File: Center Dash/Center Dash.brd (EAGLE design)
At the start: 159 x 86.7 mm, 82 parts, among them J1 502585-0470, Q1 BSS138, Q2 BSS138, Q3 BSS138, Q4 BSS138, U1 ADG3304BRUZ-REEL7, U2 TPS54540DDARQ1

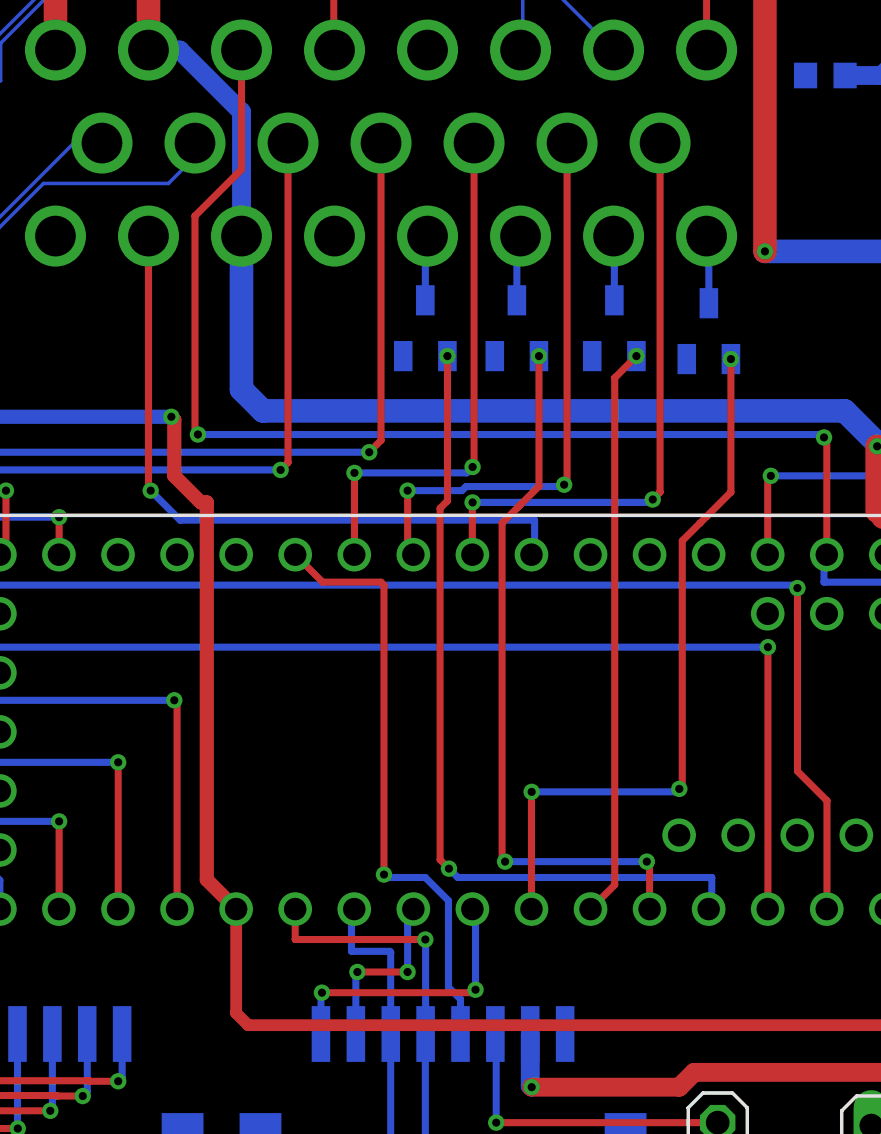
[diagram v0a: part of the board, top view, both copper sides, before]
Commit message: Add voltage dividers to 5V input lines
Now we can use Teensy 3.6
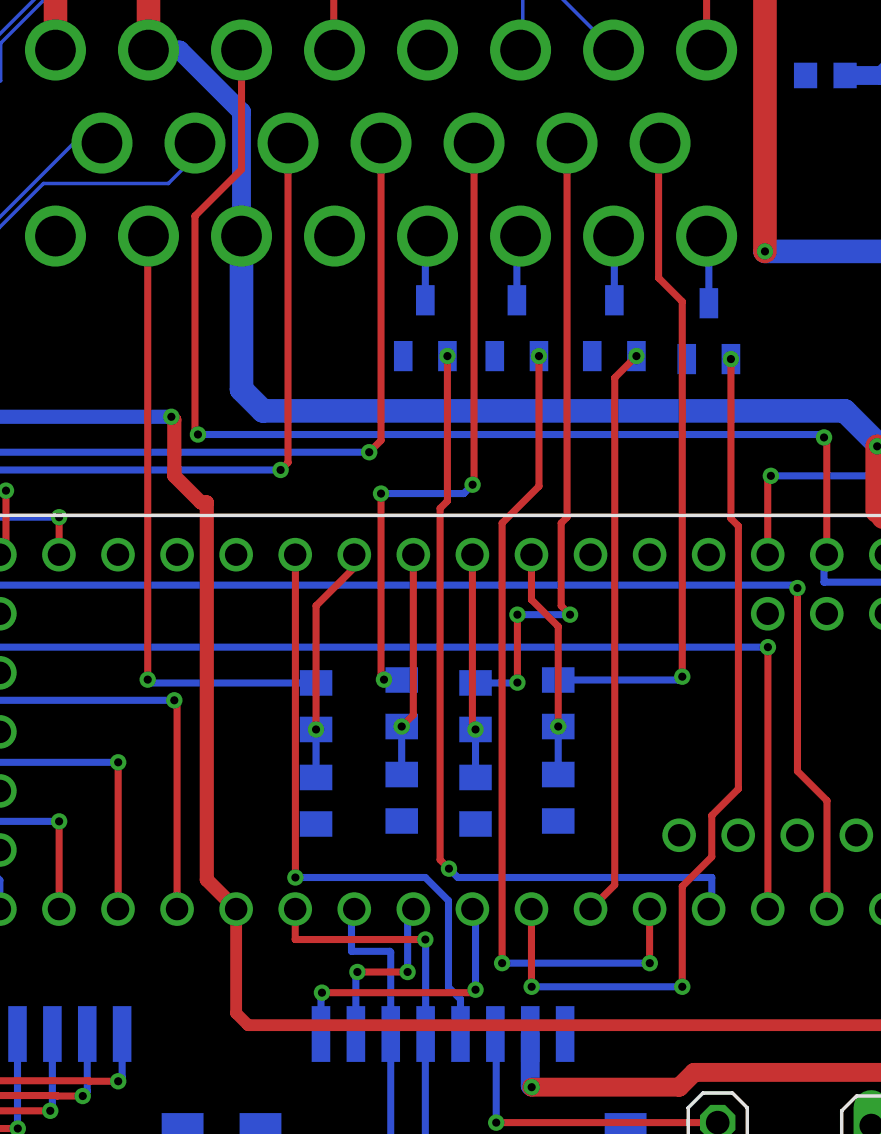
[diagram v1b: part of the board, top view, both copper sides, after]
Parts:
- added R17, R19, R21, R23: 1K, adafruit:R0805
- added R18, R20, R22, R24: 2K, adafruit:R0805
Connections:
- new net SW_BIT0_IN: R17.2, U$1.P$17
- new net SW_BIT1_IN: R19.2, U$1.P$13
- new net SW_BIT2_IN: R21.2, U$1.P$14
- new net SW_BIT3_IN: R23.2, U$1.P$15
- net GND: now also R18.1, R20.1, R22.1, R24.1
- net SW_BIT0: now also R17.1, R18.2; no longer U$1.P$13
- net SW_BIT1: now also R19.1, R20.2; no longer U$1.P$14
- net SW_BIT2: now also R21.1, R22.2; no longer U$1.P$15
- net SW_BIT3: now also R23.1, R24.2; no longer U$1.P$17
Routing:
- net SW_BIT3_IN: track 0.00 -> 28.8 mm, vias 0 -> 1
- net SW_BIT1_IN: track 0.00 -> 27.6 mm, vias 0 -> 3
- net SW_BIT2_IN: track 0.00 -> 27.5 mm, vias 0 -> 3
- net SW_BIT0_IN: track 0.00 -> 26.4 mm, vias 0 -> 1
- net SW_BIT3: track 29.6 -> 9.93 mm
- net SW_BIT2: track 25.5 -> 9.64 mm, vias 2 -> 1
- net SW_BIT1: track 24.4 -> 9.66 mm, vias 2 -> 1
- net SW_BIT0: track 22.7 -> 10.3 mm, vias 2 -> 1
- net TPS: track 30.9 -> 37.9 mm
- net IMD: track 30.6 -> 35.4 mm
- net CLK: track 26.0 -> 26.8 mm

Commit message: last minute fix again
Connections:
- net +3V3: now also U1.8
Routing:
- net +3V3: track 180.1 -> 188.9 mm
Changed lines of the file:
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@@
 <wire x1="-28.067" y1="74.422" x2="-28.067" y2="76.134" width="0.6096" layer="16"/>
 <wire x1="-28.067" y1="76.134" x2="-28.895" y2="76.962" width="0.6096" layer="16"/>
+<contactref element="U1" pad="8"/>
+<wire x1="38.252" y1="59.608" x2="36.494" y2="59.608" width="0.3048" layer="16"/>
+<wire x1="36.494" y1="59.608" x2="35.814" y2="58.928" width="0.3048" layer="16"/>
+<wire x1="35.814" y1="58.928" x2="35.814" y2="57.658" width="0.3048" layer="16"/>
+<wire x1="35.814" y1="57.658" x2="34.671" y2="56.515" width="0.3048" layer="16"/>
+<wire x1="34.671" y1="56.515" x2="34.417" y2="56.261" width="0.3048" layer="16"/>
+<wire x1="31.852" y1="55.708" x2="33.864" y2="55.708" width="0.3048" layer="16"/>
+<wire x1="33.864" y1="55.708" x2="34.417" y2="56.261" width="0.3048" layer="16"/>
 </signal>
 <signal name="PADDLE">
@@
 <wire x1="36.957" y1="52.578" x2="36.957" y2="57.277" width="0.3048" layer="1"/>
 <wire x1="36.957" y1="57.277" x2="35.941" y2="58.293" width="0.3048" layer="1"/>
-<via x="35.941" y="58.293" extent="1-16" drill="0.35"/>
-<wire x1="35.941" y1="58.293" x2="31.867" y2="58.293" width="0.3048" layer="16"/>
-<wire x1="31.867" y1="58.293" x2="31.852" y2="58.308" width="0.3048" layer="16"/>
+<wire x1="35.941" y1="58.293" x2="35.9184" y2="58.2704" width="0.3048" layer="1"/>
+<wire x1="35.9184" y1="58.2704" x2="34.544" y2="58.2704" width="0.3048" layer="1"/>
+<via x="34.544" y="58.2704" extent="1-16" drill="0.35"/>
+<wire x1="34.544" y1="58.2704" x2="31.8896" y2="58.2704" width="0.3048" layer="16"/>
+<wire x1="31.8896" y1="58.2704" x2="31.852" y2="58.308" width="0.3048" layer="16"/>
 </signal>
 <signal name="DI">
@@
 <wire x1="30.226" y1="63.5" x2="30.419" y2="63.693" width="0.3048" layer="1"/>
 <wire x1="30.419" y1="63.693" x2="31.877" y2="63.693" width="0.3048" layer="1"/>
-<via x="36.83" y="58.928" extent="1-16" drill="0.35"/>
-<wire x1="36.83" y1="58.928" x2="36.8" y2="58.958" width="0.3048" layer="16"/>
-<wire x1="36.8" y1="58.958" x2="31.852" y2="58.958" width="0.3048" layer="16"/>
 <contactref element="JP5" pad="1"/>
 <wire x1="39.497" y1="52.578" x2="39.497" y2="58.801" width="0.3048" layer="1"/>
 <wire x1="39.497" y1="58.801" x2="39.37" y2="58.928" width="0.3048" layer="1"/>
-<wire x1="39.37" y1="58.928" x2="36.83" y2="58.928" width="0.3048" layer="1"/>
+<via x="33.655" y="58.928" extent="1-16" drill="0.35"/>
+<wire x1="33.655" y1="58.928" x2="33.625" y2="58.958" width="0.3048" layer="16"/>
+<wire x1="33.625" y1="58.958" x2="31.852" y2="58.958" width="0.3048" layer="16"/>
+<wire x1="39.37" y1="58.928" x2="33.655" y2="58.928" width="0.3048" layer="1"/>
 </signal>
 <signal name="DI_MORE">

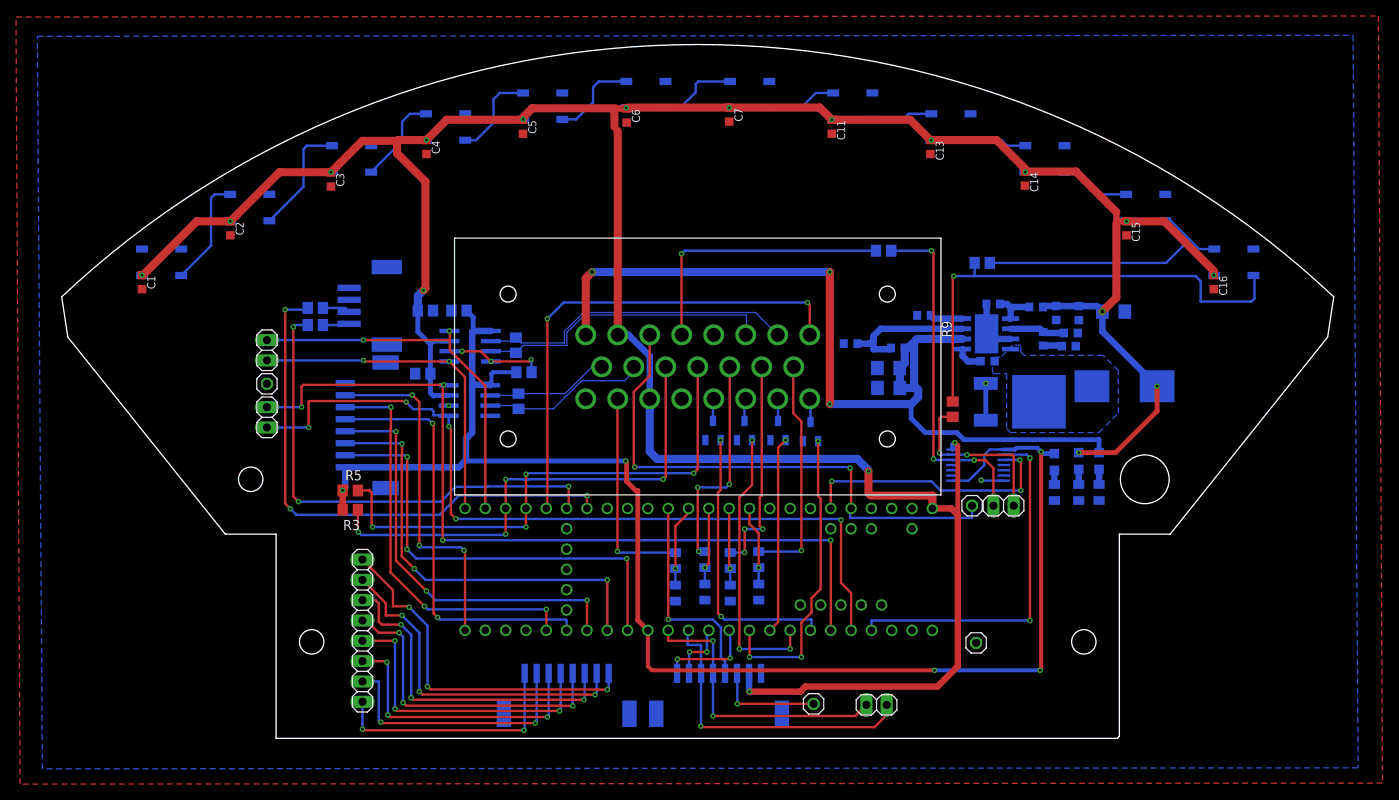
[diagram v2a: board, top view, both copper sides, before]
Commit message: Fixed?? amp seal connector
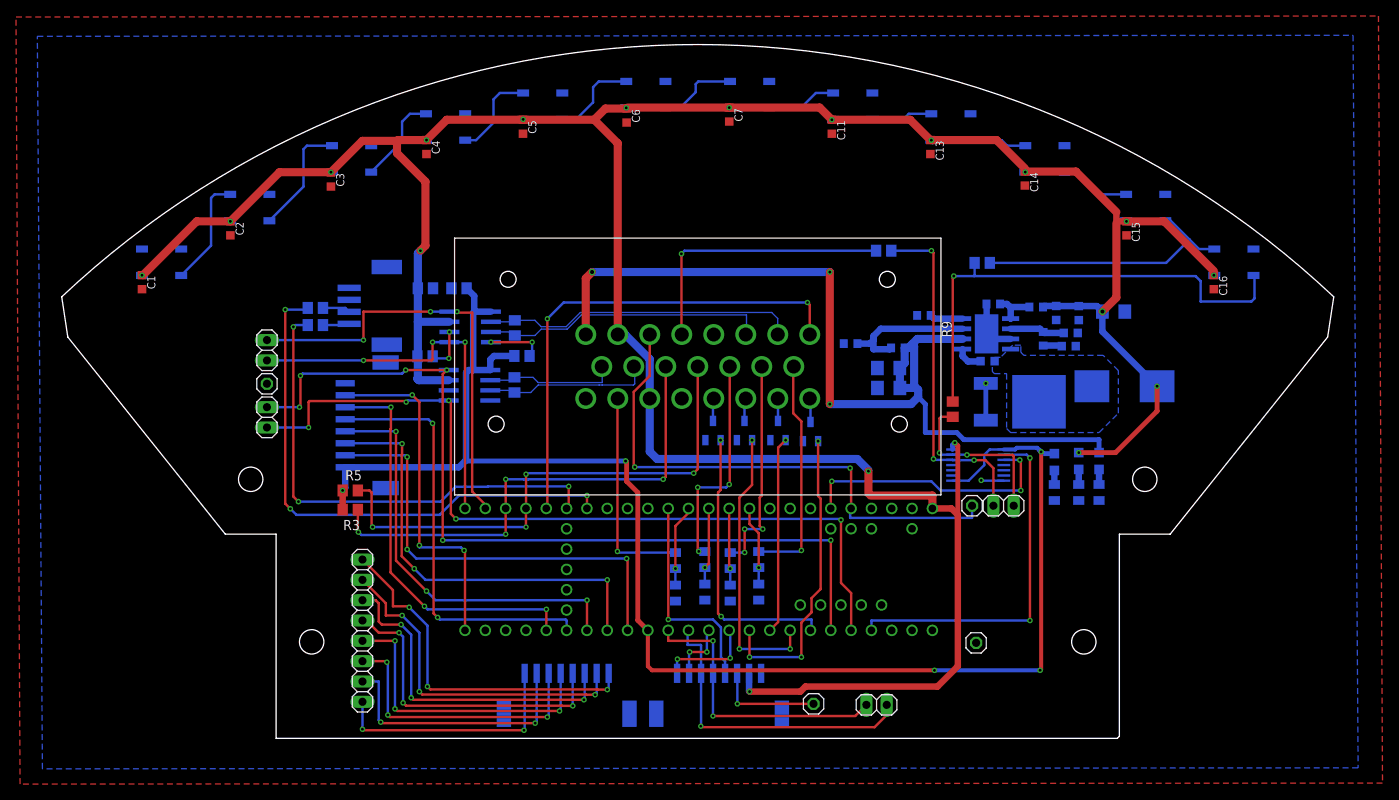
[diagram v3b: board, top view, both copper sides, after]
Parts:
- U$1: device FormE:776200-1 -> FormE:TE-776200-1
- moved C17 2.79 mm to (-34.0, 79.8)
- moved C21 2.79 mm to (-29.8, 79.8)
- moved U4 2.41 mm to (-28.4, 74.9)
- moved C19 2.18 mm to (-34.1, 71.2), turned to 180 degrees
- moved R16 2.16 mm to (-22.9, 74.8)
- moved R4 2.09 mm to (-22.9, 67.7)
- moved C20 2.05 mm to (-22.0, 71.3)
- moved U3 1.91 mm to (-28.5, 67.6)
- turned U$1 to 0 degrees
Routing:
- net DAQCAN_RX: track 46.9 -> 54.4 mm, vias 2 -> 3
- net DAQCAN_TX: track 42.0 -> 47.9 mm, vias 2 -> 3
- net CARCAN_RX: track 104.8 -> 108.1 mm, vias 4 -> 6
- net +3V3: track 188.9 -> 191.5 mm
- net DAQCAN_P: track 37.5 -> 35.7 mm
- net CARCAN_N: track 15.4 -> 16.4 mm
- net GND: track 27.0 -> 28.0 mm
- net CARCAN_TX: track 102.8 -> 103.8 mm
- net DAQCAN_N: track 39.9 -> 39.3 mm

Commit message: Rotate LEDs. Might fit better??
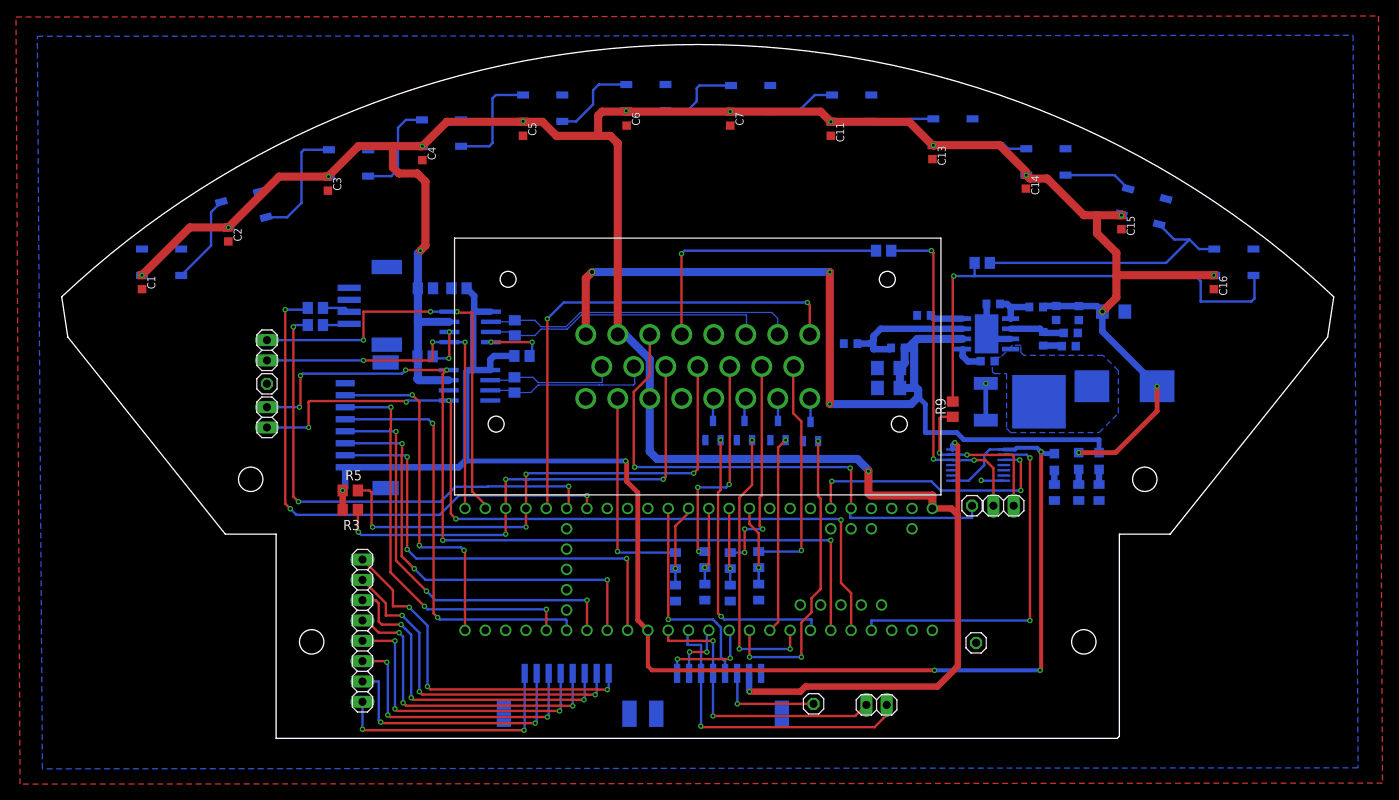
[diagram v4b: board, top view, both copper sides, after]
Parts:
- moved C15 0.99 mm to (53.0, 88.0)
- moved C4 0.92 mm to (-34.4, 96.6)
- moved LED9 0.92 mm to (-32.0, 99.2)
- moved C2 0.80 mm to (-58.7, 86.5)
- moved LED11 0.80 mm to (-56.8, 89.6), turned to 345 degrees
- moved C13 0.68 mm to (29.3, 96.8)
- moved LED4 0.68 mm to (31.9, 99.3)
- moved C3 0.63 mm to (-46.2, 92.8)
- moved LED10 0.63 mm to (-43.6, 95.4)
- moved LED6 0.52 mm to (6.61, 103.5)
- moved C7 0.52 mm to (4.06, 101.0)
- moved C14 0.40 mm to (41.0, 93.1)
- moved LED3 0.40 mm to (43.5, 95.5)
- moved C6 0.38 mm to (-8.89, 101.0)
- moved LED7 0.38 mm to (-6.49, 103.6)
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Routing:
- net N$40: track 13.8 -> 11.3 mm
- net N$37: track 11.4 -> 13.7 mm
- net N$38: track 11.3 -> 12.7 mm
- net N$39: track 14.5 -> 15.1 mm
- net N$2: track 33.8 -> 34.3 mm
- net N$6: track 7.66 -> 8.20 mm
- net N$8: track 10.0 -> 10.5 mm
